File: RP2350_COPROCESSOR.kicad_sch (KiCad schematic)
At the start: 32 parts, among them J2 M50-3530542, SW6 SW_Push, SW7 SW_Push, U2 RP2350A, U26 W25Q128JVSIQ, Y6 ABM8-272-T3_12MHZ

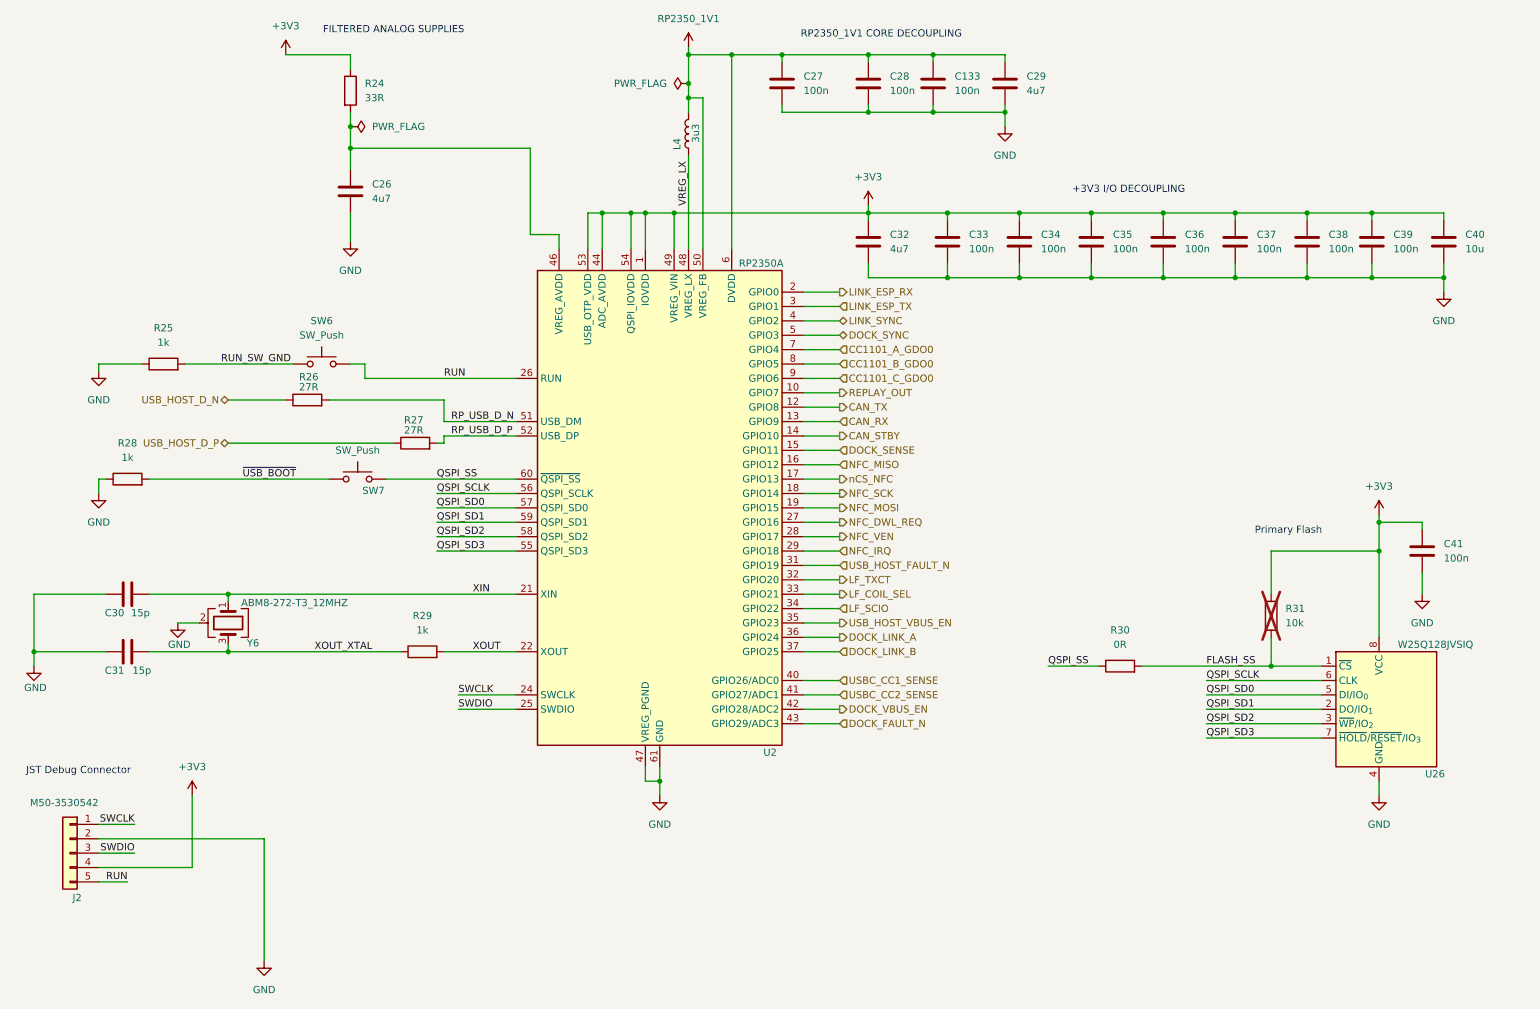
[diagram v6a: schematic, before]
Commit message: changiong bootsel buttom in rp
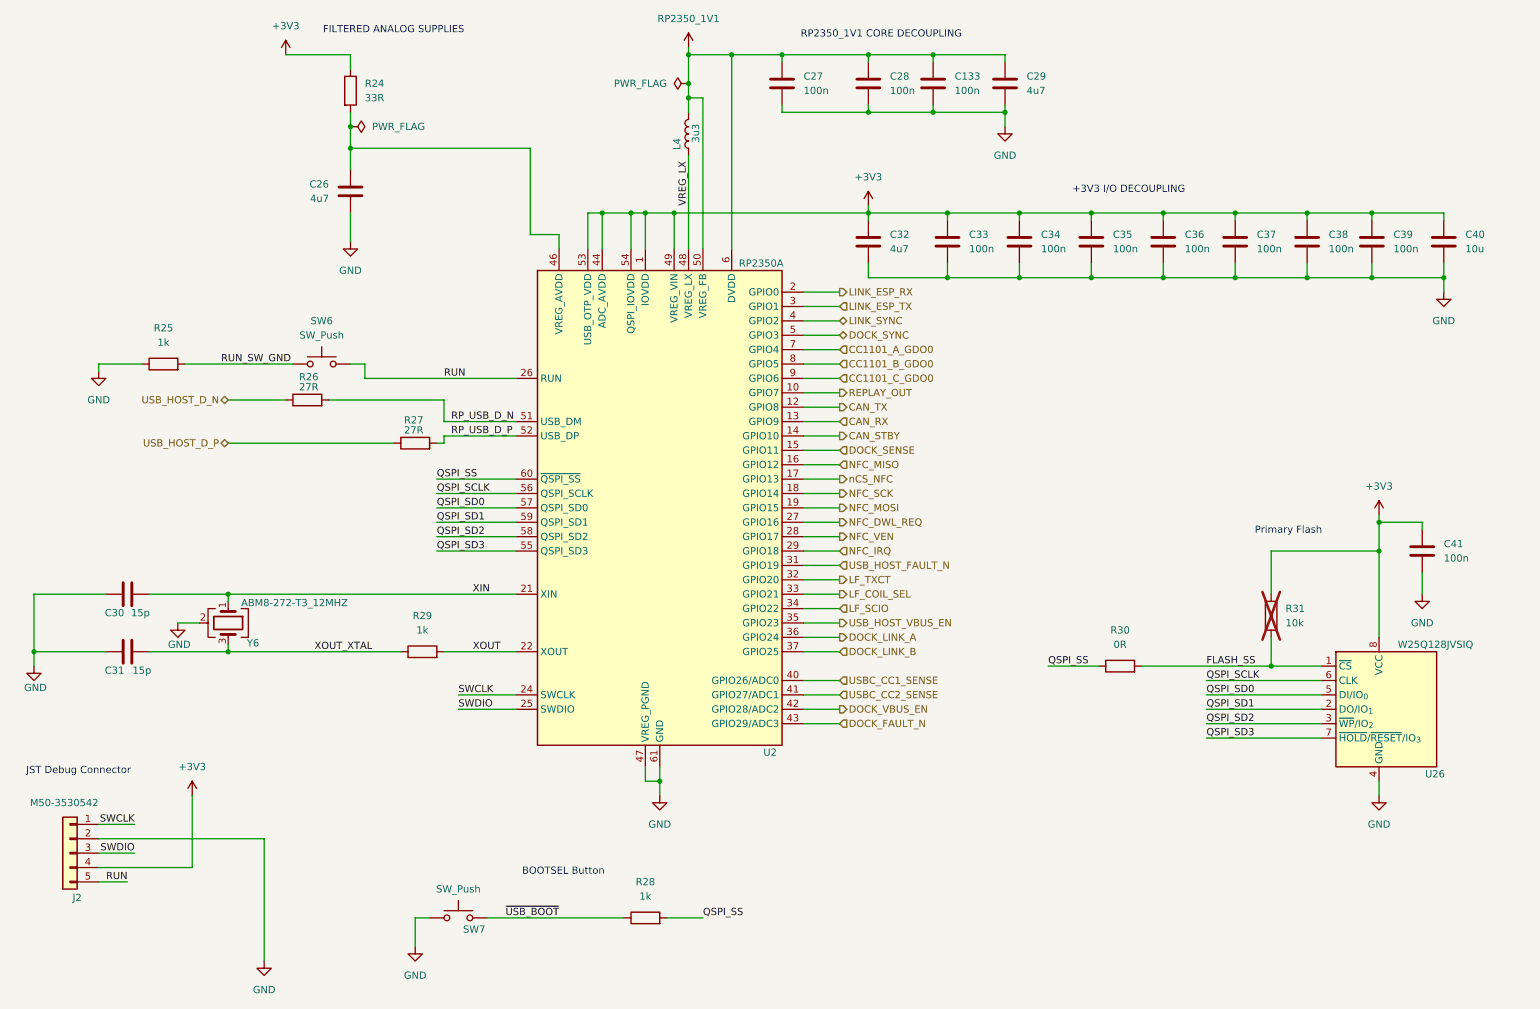
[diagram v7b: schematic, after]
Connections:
- net GND: now also SW7.1; no longer R28.1
- net QSPI_SS: now also R28.2; no longer SW7.2
- net ~{USB_BOOT}: now also R28.1, SW7.2; no longer R28.2, SW7.1
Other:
- note added: "BOOTSEL Button"

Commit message: nearly finishing placement phase
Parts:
- added C175: 100n, Capacitor_SMD:C_0402_1005Metric, symbol Device:C
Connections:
- net +3V3: now also C175.1
- net GND: now also C175.2
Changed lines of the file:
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@@
 	)
 	(junction
+		(at 270.51 48.26)
+		(diameter 0)
+		(color 0 0 0 0)
+	)
+	(junction
 		(at 208.28 48.26)
 		(diameter 0)
@@
 	)
 	(junction
+		(at 280.67 59.69)
+		(diameter 0)
+		(color 0 0 0 0)
+	)
+	(junction
 		(at 137.16 25.4)
 		(diameter 0)
@@
 	(wire
 		(pts
+			(xy 280.67 49.53) (xy 280.67 48.26)
+		)
+		(stroke
+			(width 0)
+			(type default)
+		)
+	)
+	(wire
+		(pts
 			(xy 80.01 77.47) (xy 80.01 74.93)
 		)
@@
 	(wire
 		(pts
-			(xy 270.51 59.69) (xy 270.51 62.23)
+			(xy 280.67 59.69) (xy 280.67 62.23)
 		)
 		(stroke
@@
 	(wire
 		(pts
+			(xy 280.67 59.69) (xy 270.51 59.69)
+		)
+		(stroke
+			(width 0)
+			(type default)
+		)
+	)
+	(wire
+		(pts
 			(xy 129.54 148.59) (xy 132.08 148.59)
 		)
@@
 	(wire
 		(pts
+			(xy 280.67 48.26) (xy 270.51 48.26)
+		)
+		(stroke
+			(width 0)
+			(type default)
+		)
+	)
+	(wire
+		(pts
 			(xy 157.48 115.57) (xy 163.83 115.57)
 		)
@@
 	(wire
 		(pts
+			(xy 280.67 57.15) (xy 280.67 59.69)
+		)
+		(stroke
+			(width 0)
+			(type default)
+		)
+	)
+	(wire
+		(pts
 			(xy 33.02 158.75) (xy 62.23 158.75)
 		)
@@
 	(symbol
 		(lib_id "power:GND")
-		(at 270.51 62.23 0)
+		(at 280.67 62.23 0)
 		(unit 1)
 		(body_style 1)
@@
 		(fields_autoplaced yes)
 		(property "Reference" "#PWR046"
-			(at 270.51 68.58 0)
+			(at 280.67 68.58 0)
 			(hide yes)
 			(show_name no)
@@
 		)
 		(property "Value" "GND"
-			(at 270.51 67.31 0)
+			(at 280.67 67.31 0)
 			(show_name no)
 			(do_not_autoplace no)
@@
 		)
 		(property "Footprint" ""
-			(at 270.51 62.23 0)
+			(at 280.67 62.23 0)
 			(hide yes)
 			(show_name no)
@@
 		)
 		(property "Datasheet" ""
-			(at 270.51 62.23 0)
+			(at 280.67 62.23 0)
 			(hide yes)
 			(show_name no)
@@
 		)
 		(property "Description" "Power symbol creates a global label with name \"GND\" , ground"
-			(at 270.51 62.23 0)
+			(at 280.67 62.23 0)
 			(hide yes)
 			(show_name no)
@@
 					(unit 1)
 				)
+			)
+		)
+	)
+	(symbol
+		(lib_id "Device:C")
+		(at 280.67 53.34 0)
+		(unit 1)
+		(body_style 1)
+		(exclude_from_sim no)
+		(in_bom yes)
+		(on_board yes)
+		(in_pos_files yes)
+		(dnp no)
+		(property "Reference" "C175"
+			(at 280.924 51.054 0)
+			(show_name no)
+			(do_not_autoplace no)
+			(effects
+				(font
+					(size 1.016 1.016)
+				)
+				(justify left)
+			)
+		)
+		(property "Value" "100n"
+			(at 280.924 55.372 0)
+			(show_name no)
+			(do_not_autoplace no)
+			(effects
+				(font
+					(size 1.016 1.016)
+				)
+				(justify left)
+			)
+		)
+		(property "Footprint" "Capacitor_SMD:C_0402_1005Metric"
+			(at 281.6352 57.15 0)
+			(hide yes)
+			(show_name no)
+			(do_not_autoplace no)
+			(effects
+				(font
+					(size 1.27 1.27)
+				)
+			)
+		)
+		(property "Datasheet" "https://pim.murata.com/en-global/pim/details/?partNum=GRM155R71C104KA88D"
+			(at 280.67 53.34 0)
+			(hide yes)
+			(show_name no)
+			(do_not_autoplace no)
+			(effects
+				(font
+					(size 1.27 1.27)
+				)
+			)
+		)
+		(property "Description" "Unpolarized capacitor"
+			(at 280.67 53.34 0)
+			(hide yes)
+			(show_name no)
+			(do_not_autoplace no)
+			(effects
+				(font
+					(size 1.27 1.27)
+				)
+			)
+		)
+		(property "DISTRIBUTOR_LINK" "https://www.mouser.com/ProductDetail/Murata-Electronics/GRM155R71C104KA88D?qs=8YPuuxuUzMJKePo9sU3A2g%3D%3D"
+			(at 280.67 53.34 0)
+			(hide yes)
+			(show_name no)
+			(do_not_autoplace no)
+			(effects
+				(font
+					(size 1.27 1.27)
+				)
+			)
+		)
+		(property "MPN" "GRM155R71C104KA88D"
+			(at 280.67 53.34 0)
+			(hide yes)
+			(show_name no)
+			(do_not_autoplace no)
+			(effects
+				(font
+					(size 1.27 1.27)
+				)
+			)
+		)
+		(property "KLC_S3.3" ""
+			(at 280.67 53.34 0)
+			(hide yes)
+			(show_name no)
+			(do_not_autoplace no)
+			(effects
+				(font
+					(size 1.27 1.27)
+				)
+			)
+		)
+		(property "KLC_S4.1" ""
+			(at 280.67 53.34 0)
+			(hide yes)
+			(show_name no)
+			(do_not_autoplace no)
+			(effects
+				(font
+					(size 1.27 1.27)
+				)
+			)
+		)
+		(property "KLC_S4.2_DVDD" ""
+			(at 280.67 53.34 0)
+			(hide yes)
+			(show_name no)
+			(do_not_autoplace no)
+			(effects
+				(font
+					(size 1.27 1.27)
+				)
+			)
+		)
+		(property "KLC_S4.2_VREG_LX" ""
+			(at 280.67 53.34 0)
+			(hide yes)
+			(show_name no)
+			(do_not_autoplace no)
+			(effects
+				(font
+					(size 1.27 1.27)
+				)
+			)
+		)
+		(property "Notes" "N/A"
+			(at 280.67 53.34 0)
+			(hide yes)
+			(show_name no)
+			(do_not_autoplace no)
+			(effects
+				(font
+					(size 1.27 1.27)
+				)
+			)
+		)
+		(property "MANUFACTURER" "Murata"
+			(at 280.67 53.34 0)
+			(hide yes)
+			(show_name no)
+			(do_not_autoplace no)
+			(effects
+				(font
+					(size 1.27 1.27)
+				)
+			)
+		)
+		(property "TUNING_ALTERNATIVES" ""
+			(at 280.67 53.34 0)
+			(hide yes)
+			(show_name no)
+			(do_not_autoplace no)
+			(effects
+				(font
+					(size 1.27 1.27)
+				)
+			)
+		)
+		(pin "2"
+		)
+		(pin "1"
+		)
+		(instances
+			(project "FOBtool_HW"
+				(path "/4178b7d0-cf29-4cf2-b214-acbbbd97d338/27b7c62f-0663-47bb-bbed-fbdc5a64ed05"
+					(reference "C175")
+					(unit 1)
+				)
